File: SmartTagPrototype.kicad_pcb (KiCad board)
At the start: 2 copper layers, 57 x 31 mm, 50 parts, among them IC1 NRF52810-QFAA-R7, IC3 AEM30940-QFN, J1 Nordic output antenna, J7 Additional AC pins, J8 Conn_Coaxial, J9 AC pins (generator/antenna), X1 32MHz

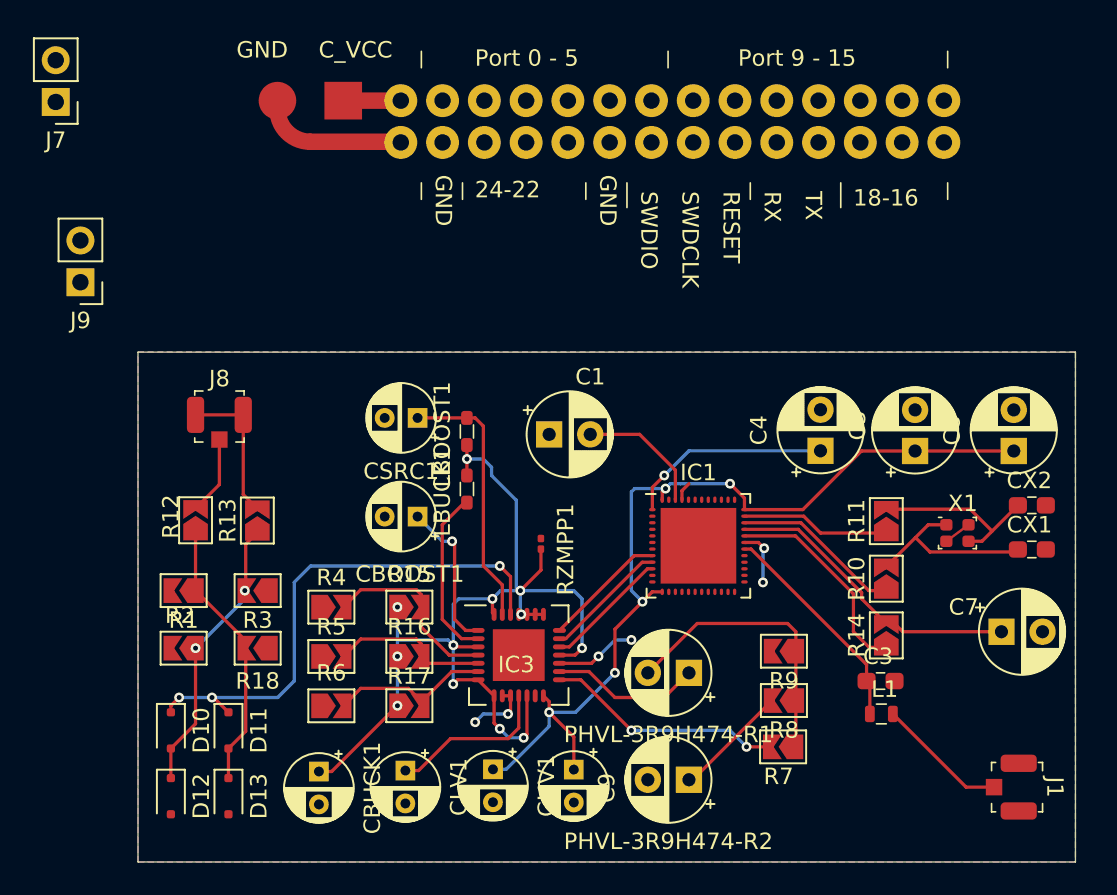
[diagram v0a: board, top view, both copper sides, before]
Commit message: diag dodany, finish /PCB
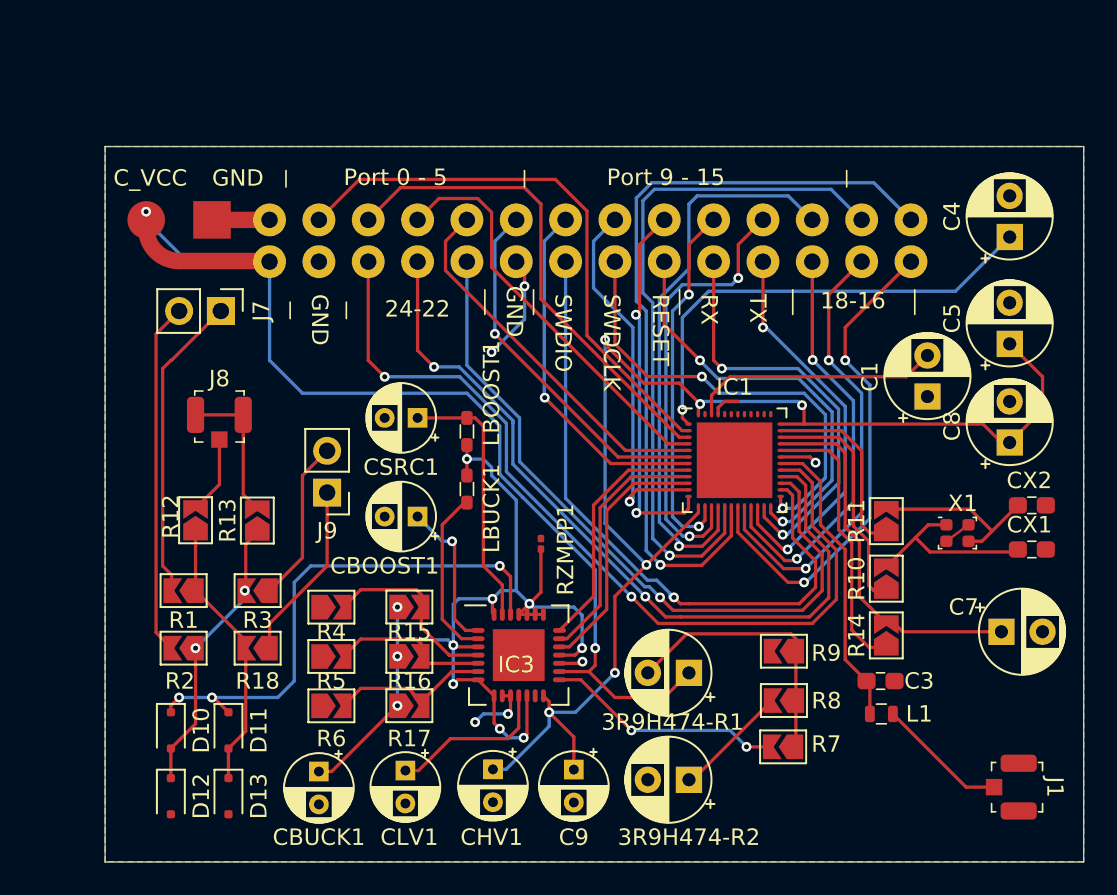
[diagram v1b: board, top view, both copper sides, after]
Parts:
- moved C1 23.1 mm to (136.5, 87.2), turned to 90 degrees
- moved J9 19.7 mm to (100.0, 93.0)
- moved C4 17.4 mm to (141.5, 77.5)
- moved J7 16.2 mm to (93.5, 82.0), turned to -90 degrees
- moved DIAG1 10.8 mm to (107.5, 78.0)
- moved C5 8.69 mm to (141.5, 84.0)
- moved IC1 5.65 mm to (124.8, 91.1)
- moved C8 0.57 mm to (141.5, 90.0)
- renumbered PHVL-3R9H474-R1 to 3R9H474-R1, PHVL-3R9H474-R2 to 3R9H474-R2
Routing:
- net Net-(DIAG1-Port_24): track 0.00 -> 53.4 mm, vias 0 -> 2
- net Net-(DIAG1-Port_23): track 0.00 -> 48.3 mm, vias 0 -> 2
- net Net-(DIAG1-C_vol_VCC): track 9.15 -> 57.4 mm, vias 0 -> 2
- net Net-(DIAG1-Port_15): track 0.00 -> 47.8 mm, vias 0 -> 1
- net Net-(DIAG1-Port_22): track 0.00 -> 44.0 mm, vias 0 -> 1
- net Net-(DIAG1-Port_14): track 0.00 -> 42.2 mm, vias 0 -> 1
- net Net-(DIAG1-Port_26_SWDIO): track 0.00 -> 39.8 mm, vias 0 -> 1
- net Net-(DIAG1-Port_13): track 0.00 -> 35.0 mm, vias 0 -> 1
- net Net-(DIAG1-Port_0): track 0.00 -> 34.3 mm
- net Net-(DIAG1-Port_16): track 0.00 -> 30.4 mm, vias 0 -> 2
- net Net-(DIAG1-Port_1): track 0.00 -> 30.0 mm
- net Net-(DIAG1-Port_17): track 0.00 -> 27.9 mm, vias 0 -> 2
- net Net-(DIAG1-Port_25_SWDCLK): track 0.00 -> 27.6 mm, vias 0 -> 2
- net Net-(DIAG1-Port_12): track 0.00 -> 27.1 mm, vias 0 -> 2
- net Net-(DIAG1-Port_20_RX): track 0.00 -> 26.2 mm, vias 0 -> 2
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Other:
- board size 57 x 31 mm -> 59.5 x 43.5 mm
